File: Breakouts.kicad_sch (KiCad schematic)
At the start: 21 parts, among them J1 Conn_01x08, J10 AudioJack3_Switch, J11 Conn_01x03, J12 Conn_01x03, J13 Barrel_Jack_Switch, J14 Conn_01x03, J15 Conn_01x08, J16 Conn_01x08, J2 Conn_01x08, J3 Conn_01x08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

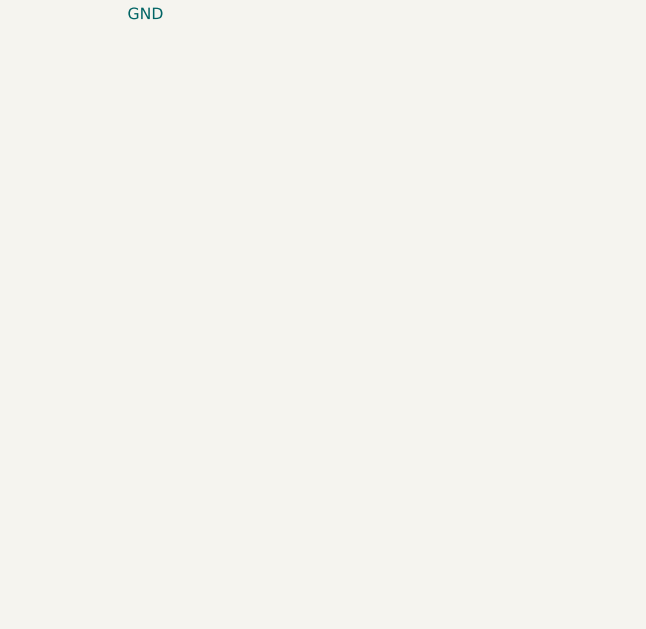
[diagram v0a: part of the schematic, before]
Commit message: Add schematic for pos18 ffc cable
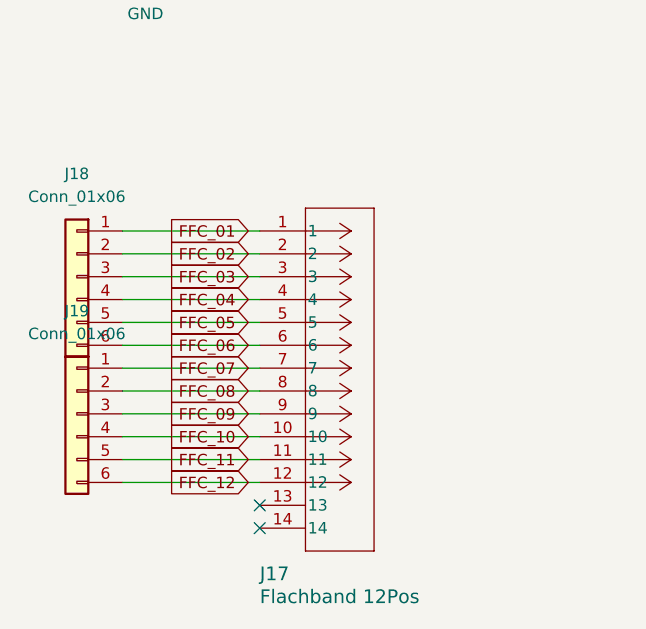
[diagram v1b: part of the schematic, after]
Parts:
- added J17: Flachband 12Pos, CONN12_1-1734742-2_TEC, symbol 2024-04-23_17-15-49:1-1734742-2
- added J18, J19: Conn_01x06, Connector_PinHeader_2.54mm:PinHeader_1x06_P2.54mm_Vertical, symbol Connector_Generic:Conn_01x06
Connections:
- new net FFC_01: J17.1, J18.1 (Pin_1)
- new net FFC_02: J17.2, J18.2 (Pin_2)
- new net FFC_03: J17.3, J18.3 (Pin_3)
- new net FFC_04: J17.4, J18.4 (Pin_4)
- new net FFC_05: J17.5, J18.5 (Pin_5)
- new net FFC_06: J17.6, J18.6 (Pin_6)
- new net FFC_07: J17.7, J19.1 (Pin_1)
- new net FFC_08: J17.8, J19.2 (Pin_2)
- new net FFC_09: J17.9, J19.3 (Pin_3)
- new net FFC_10: J17.10, J19.4 (Pin_4)
- new net FFC_11: J17.11, J19.5 (Pin_5)
- new net FFC_12: J17.12, J19.6 (Pin_6)
- no-connect marks 17 -> 19
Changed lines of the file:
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@@
   (no_connect (at 190.5 59.055))
   (no_connect (at 264.16 49.53))
+  (no_connect (at 68.58 149.86))
   (no_connect (at 200.66 59.055))
   (no_connect (at 195.58 59.055))
+  (no_connect (at 68.58 152.4))
   (no_connect (at 266.7 49.53))
   (no_connect (at 266.7 27.94))
   (no_connect (at 198.12 59.055))
+  (wire (pts (xy 68.58 144.78) (xy 53.34 144.78))
+    (stroke (width 0) (type default))
+  )
   (wire (pts (xy 184.15 118.11) (xy 173.99 118.11))
     (stroke (width 0) (type default))
   )
+  (wire (pts (xy 68.58 124.46) (xy 53.34 124.46))
+    (stroke (width 0) (type default))
+  )
   (wire (pts (xy 259.08 29.21) (xy 259.08 27.94))
     (stroke (width 0) (type default))
@@
     (stroke (width 0) (type default))
   )
+  (wire (pts (xy 68.58 129.54) (xy 53.34 129.54))
+    (stroke (width 0) (type default))
+  )
   (wire (pts (xy 259.08 31.75) (xy 259.08 33.02))
     (stroke (width 0) (type default))
@@
     (stroke (width 0) (type default))
   )
+  (wire (pts (xy 68.58 127) (xy 53.34 127))
+    (stroke (width 0) (type default))
+  )
   (wire (pts (xy 57.15 78.74) (xy 57.15 73.66))
     (stroke (width 0) (type default))
@@
     (stroke (width 0) (type default))
   )
+  (wire (pts (xy 68.58 139.7) (xy 53.34 139.7))
+    (stroke (width 0) (type default))
+  )
   (wire (pts (xy 261.62 33.02) (xy 261.62 29.21))
     (stroke (width 0) (type default))
@@
     (stroke (width 0) (type default))
   )
+  (wire (pts (xy 68.58 134.62) (xy 53.34 134.62))
+    (stroke (width 0) (type default))
+  )
   (wire (pts (xy 260.35 114.3) (xy 266.7 114.3))
     (stroke (width 0) (type default))
@@
     (stroke (width 0) (type default))
   )
+  (wire (pts (xy 68.58 142.24) (xy 53.34 142.24))
+    (stroke (width 0) (type default))
+  )
   (wire (pts (xy 57.15 73.66) (xy 58.42 73.66))
     (stroke (width 0) (type default))
@@
     (stroke (width 0) (type default))
   )
+  (wire (pts (xy 68.58 132.08) (xy 53.34 132.08))
+    (stroke (width 0) (type default))
+  )
   (wire (pts (xy 266.7 101.6) (xy 264.16 101.6))
     (stroke (width 0) (type default))
   )
+  (wire (pts (xy 68.58 119.38) (xy 53.34 119.38))
+    (stroke (width 0) (type default))
+  )
   (wire (pts (xy 81.28 78.74) (xy 76.2 78.74))
     (stroke (width 0) (type default))
@@
     (stroke (width 0) (type default))
   )
+  (wire (pts (xy 68.58 147.32) (xy 53.34 147.32))
+    (stroke (width 0) (type default))
+  )
   (wire (pts (xy 266.7 99.06) (xy 256.54 99.06))
     (stroke (width 0) (type default))
@@
   (wire (pts (xy 256.54 101.6) (xy 261.62 101.6))
     (stroke (width 0) (type default))
+  )
+  (wire (pts (xy 68.58 121.92) (xy 53.34 121.92))
+    (stroke (width 0) (type default))
+  )
+  (wire (pts (xy 68.58 137.16) (xy 53.34 137.16))
+    (stroke (width 0) (type default))
+  )
+  (global_label "FFC_02" (shape input) (at 67.31 121.92 180) (fields_autoplaced)
+    (effects (font (size 1.27 1.27)) (justify right))
+    (property "Intersheetrefs" "${INTERSHEET_REFS}" (at 57.491 121.92 0)
+      (effects (font (size 1.27 1.27)) (justify right) hide)
+    )
+  )
+  (global_label "FFC_08" (shape input) (at 67.31 137.16 180) (fields_autoplaced)
+    (effects (font (size 1.27 1.27)) (justify right))
+    (property "Intersheetrefs" "${INTERSHEET_REFS}" (at 57.491 137.16 0)
+      (effects (font (size 1.27 1.27)) (justify right) hide)
+    )
   )
   (global_label "POWx" (shape input) (at 175.26 92.71 90) (fields_autoplaced)
@@
     (property "Intersheetrefs" "${INTERSHEET_REFS}" (at 175.26 84.6448 90)
       (effects (font (size 1.27 1.27)) (justify left) hide)
+    )
+  )
+  (global_label "FFC_10" (shape input) (at 67.31 142.24 180) (fields_autoplaced)
+    (effects (font (size 1.27 1.27)) (justify right))
+    (property "Intersheetrefs" "${INTERSHEET_REFS}" (at 57.491 142.24 0)
+      (effects (font (size 1.27 1.27)) (justify right) hide)
+    )
+  )
+  (global_label "FFC_03" (shape input) (at 67.31 124.46 180) (fields_autoplaced)
+    (effects (font (size 1.27 1.27)) (justify right))
+    (property "Intersheetrefs" "${INTERSHEET_REFS}" (at 57.491 124.46 0)
+      (effects (font (size 1.27 1.27)) (justify right) hide)
+    )
+  )
+  (global_label "FFC_09" (shape input) (at 67.31 139.7 180) (fields_autoplaced)
+    (effects (font (size 1.27 1.27)) (justify right))
+    (property "Intersheetrefs" "${INTERSHEET_REFS}" (at 57.491 139.7 0)
+      (effects (font (size 1.27 1.27)) (justify right) hide)
+    )
+  )
+  (global_label "FFC_04" (shape input) (at 67.31 127 180) (fields_autoplaced)
+    (effects (font (size 1.27 1.27)) (justify right))
+    (property "Intersheetrefs" "${INTERSHEET_REFS}" (at 57.491 127 0)
+      (effects (font (size 1.27 1.27)) (justify right) hide)
+    )
+  )
+  (global_label "FFC_11" (shape input) (at 67.31 144.78 180) (fields_autoplaced)
+    (effects (font (size 1.27 1.27)) (justify right))
+    (property "Intersheetrefs" "${INTERSHEET_REFS}" (at 57.491 144.78 0)
+      (effects (font (size 1.27 1.27)) (justify right) hide)
+    )
+  )
+  (global_label "FFC_06" (shape input) (at 67.31 132.08 180) (fields_autoplaced)
+    (effects (font (size 1.27 1.27)) (justify right))
+    (property "Intersheetrefs" "${INTERSHEET_REFS}" (at 57.491 132.08 0)
+      (effects (font (size 1.27 1.27)) (justify right) hide)
+    )
+  )
+  (global_label "FFC_07" (shape input) (at 67.31 134.62 180) (fields_autoplaced)
+    (effects (font (size 1.27 1.27)) (justify right))
+    (property "Intersheetrefs" "${INTERSHEET_REFS}" (at 57.491 134.62 0)
+      (effects (font (size 1.27 1.27)) (justify right) hide)
+    )
+  )
+  (global_label "FFC_12" (shape input) (at 67.31 147.32 180) (fields_autoplaced)
+    (effects (font (size 1.27 1.27)) (justify right))
+    (property "Intersheetrefs" "${INTERSHEET_REFS}" (at 57.491 147.32 0)
+      (effects (font (size 1.27 1.27)) (justify right) hide)
+    )
+  )
+  (global_label "FFC_01" (shape input) (at 67.31 119.38 180) (fields_autoplaced)
+    (effects (font (size 1.27 1.27)) (justify right))
+    (property "Intersheetrefs" "${INTERSHEET_REFS}" (at 57.491 119.38 0)
+      (effects (font (size 1.27 1.27)) (justify right) hide)
+    )
+  )
+  (global_label "FFC_05" (shape input) (at 67.31 129.54 180) (fields_autoplaced)
+    (effects (font (size 1.27 1.27)) (justify right))
+    (property "Intersheetrefs" "${INTERSHEET_REFS}" (at 57.491 129.54 0)
+      (effects (font (size 1.27 1.27)) (justify right) hide)
     )
   )
@@
     )
   )
+  (symbol (lib_id "Connector_Generic:Conn_01x06") (at 48.26 139.7 0) (mirror y) (unit 1)
+    (in_bom yes) (on_board yes) (dnp no)
+    (property "Reference" "J19" (at 48.26 128.27 0)
+      (effects (font (size 1.27 1.27)))
+    )
+    (property "Value" "Conn_01x06" (at 48.26 130.81 0)
+      (effects (font (size 1.27 1.27)))
+    )
+    (property "Footprint" "Connector_PinHeader_2.54mm:PinHeader_1x06_P2.54mm_Vertical" (at 48.26 139.7 0)
+      (effects (font (size 1.27 1.27)) hide)
+    )
+    (property "Datasheet" "~" (at 48.26 139.7 0)
+      (effects (font (size 1.27 1.27)) hide)
+    )
+    (pin "5")
+    (pin "6")
+    (pin "2")
+    (pin "1")
+    (pin "4")
+    (pin "3")
+    (instances
+      (project "Breakouts"
+        (path "/7ebf650a-1c0b-4d71-8ef1-c883cde2ac89"
+          (reference "J19") (unit 1)
+        )
+      )
+    )
+  )
   (symbol (lib_id "Connector_Generic:Conn_01x06") (at 266.7 54.61 270) (unit 1)
     (in_bom yes) (on_board yes) (dnp no) (fields_autoplaced)
@@
     )
   )
+  (symbol (lib_id "Connector_Generic:Conn_01x06") (at 48.26 124.46 0) (mirror y) (unit 1)
+    (in_bom yes) (on_board yes) (dnp no)
+    (property "Reference" "J18" (at 48.26 113.03 0)
+      (effects (font (size 1.27 1.27)))
+    )
+    (property "Value" "Conn_01x06" (at 48.26 115.57 0)
+      (effects (font (size 1.27 1.27)))
+    )
+    (property "Footprint" "Connector_PinHeader_2.54mm:PinHeader_1x06_P2.54mm_Vertical" (at 48.26 124.46 0)
+      (effects (font (size 1.27 1.27)) hide)
+    )
+    (property "Datasheet" "~" (at 48.26 124.46 0)
+      (effects (font (size 1.27 1.27)) hide)
+    )
+    (pin "5")
+    (pin "6")
+    (pin "2")
+    (pin "1")
+    (pin "4")
+    (pin "3")
+    (instances
+      (project "Breakouts"
+        (path "/7ebf650a-1c0b-4d71-8ef1-c883cde2ac89"
+          (reference "J18") (unit 1)
+        )
+      )
+    )
+  )
   (symbol (lib_id "Connector_Generic:Conn_01x06") (at 264.16 22.86 90) (unit 1)
     (in_bom yes) (on_board yes) (dnp no) (fields_autoplaced)
@@
         )
       )
+    )
+  )
+  (symbol (lib_id "2024-04-23_17-15-49:1-1734742-2") (at 68.58 119.38 0) (unit 1)
+    (in_bom yes) (on_board yes) (dnp no)
+    (property "Reference" "J17" (at 68.58 157.48 0)
+      (effects (font (size 1.524 1.524)) (justify left))
+    )
+    (property "Value" "Flachband 12Pos" (at 68.58 160.02 0)
+      (effects (font (size 1.524 1.524)) (justify left))
+    )
+    (property "Footprint" "CONN12_1-1734742-2_TEC" (at 68.58 119.38 0)
+      (effects (font (size 1.27 1.27) italic) hide)
+    )
+    (property "Datasheet" "1-1734742-2" (at 68.58 119.38 0)
+      (effects (font (size 1.27 1.27) italic) hide)
+    )
+    (pin "3")
+    (pin "4")
+    (pin "11")
+    (pin "13")
+    (pin "7")
+    (pin "12")
+    (pin "1")
+    (pin "8")
+    (pin "9")
+    (pin "5")
+    (pin "2")
+    (pin "14")
+    (pin "6")
+    (pin "10")
+    (instances
+      (project "Breakouts"
+        (path "/7ebf650a-1c0b-4d71-8ef1-c883cde2ac89"
+          (reference "J17") (unit 1)
+        )
+      )

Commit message: Merge Flachband and TDA7575B
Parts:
- added J17: Conn_01x1, Connector_PinHeader_2.54mm:PinHeader_1x14_P2.54mm_Vertical, symbol Connector_Generic:Conn_01x14
- added J18: Conn_01x14, Connector_PinHeader_2.54mm:PinHeader_1x14_P2.54mm_Vertical, symbol Connector_Generic:Conn_01x14
- added U5: TDA7575B, jlc_footprints:FLEXIWATT27-TH_27P-L29.3-W4.6-P1.00, symbol jlc_symbols:TDA7575B
- renumbered J17 to J19, J18 to J20, J19 to J21
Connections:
- net GND: now also J18.6 (Pin_6), U5.12 (SGND)
- new net: J17.1 (Pin_1), U5.1 (TAB)
- new net: J17.10 (Pin_10), U5.19 (IN2-)
- new net: J17.11 (Pin_11), U5.21 (VCC)
- new net: J17.12 (Pin_12), U5.23 (N.C.)
- new net: J17.13 (Pin_13), U5.25 (A)
- new net: J17.14 (Pin_14), U5.27 (TAB)
- new net: J17.2 (Pin_2), U5.3 (B)
- new net: J17.3 (Pin_3), U5.5 (N.C.)
- new net: J17.4 (Pin_4), U5.7 (VCC)
- new net: J17.5 (Pin_5), U5.9 (IN1-)
- new net: J17.6 (Pin_6), U5.11 (STT-BY)
- new net: J17.7 (Pin_7), U5.13 (DATA)
- new net: J17.8 (Pin_8), U5.15 (SVR)
- new net: J17.9 (Pin_9), U5.17 (1Ω)
- new net: J18.5 (Pin_5), U5.10 (MUTE)
- new net: J18.7 (Pin_7), U5.14 (CK)
- new net: J18.8 (Pin_8), U5.16 (CD_OUT)
- new net: J18.9 (Pin_9), U5.18 (I2CEN)
- new net: J18.1 (Pin_1), U5.2 (PWGND)
- new net: J18.10 (Pin_10), U5.20 (IN2+)
- new net: J18.11 (Pin_11), U5.22 (OUT2-)
- new net: J18.12 (Pin_12), U5.24 (OUT2+)
- new net: J18.13 (Pin_13), J18.14 (Pin_14), U5.26 (PWGND)
- new net: J18.2 (Pin_2), U5.4 (OUT1+)
- new net: J18.3 (Pin_3), U5.6 (OUT1-)
- new net: J18.4 (Pin_4), U5.8 (IN1+)
